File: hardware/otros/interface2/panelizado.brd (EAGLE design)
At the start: 85.9 x 92.1 mm, 40 parts

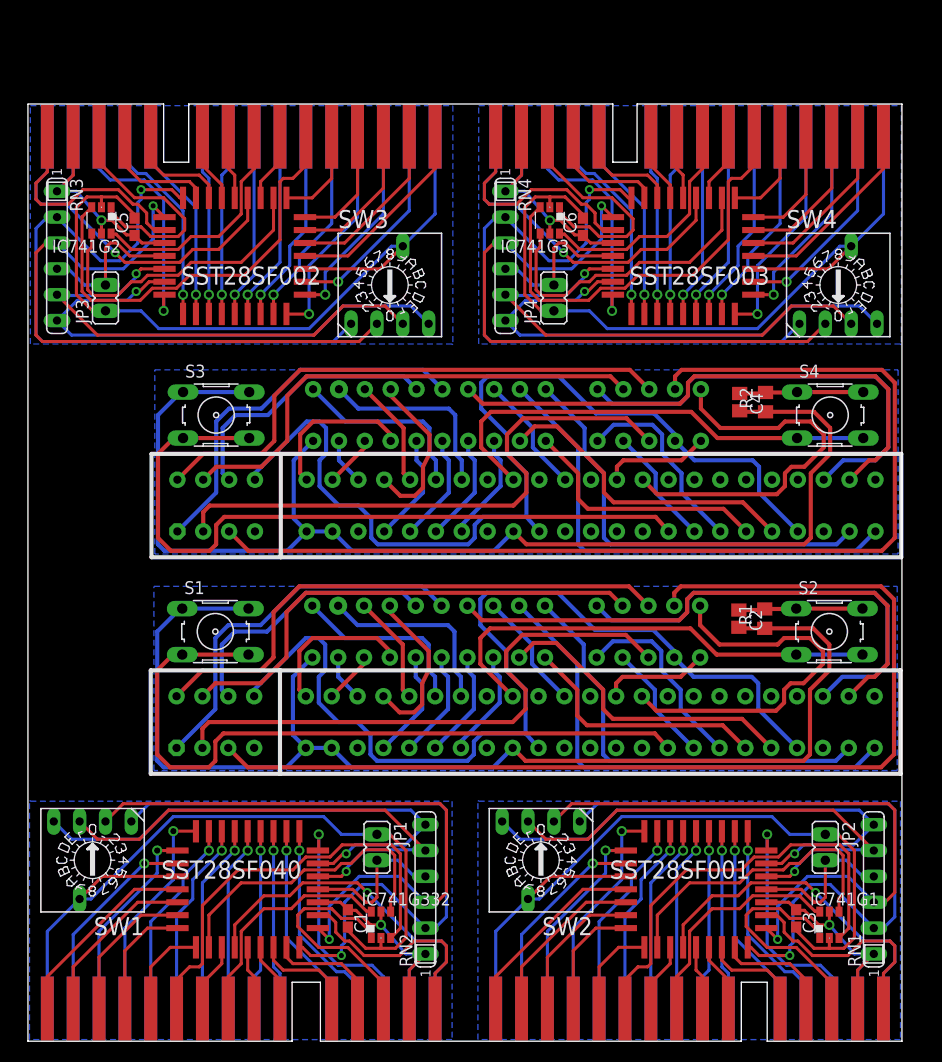
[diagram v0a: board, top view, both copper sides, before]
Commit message: 
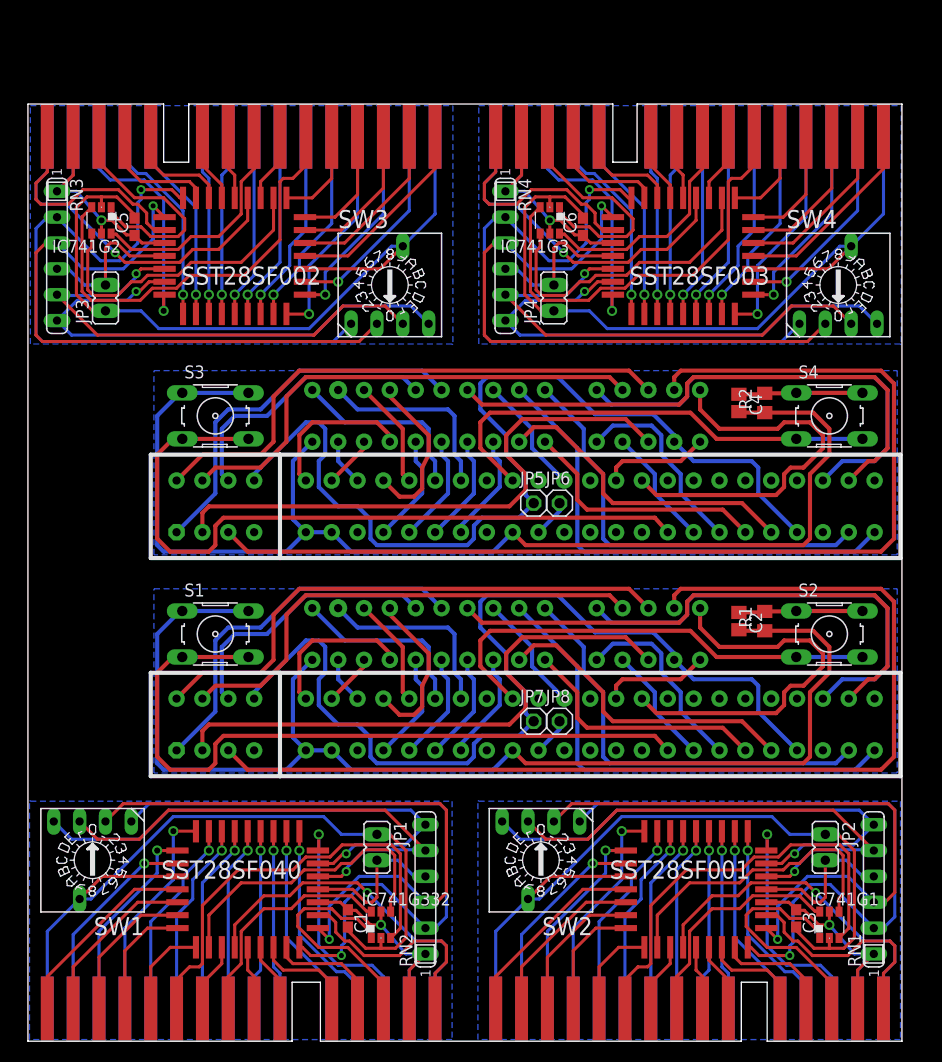
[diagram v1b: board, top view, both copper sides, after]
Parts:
- added JP5, JP6, JP7, JP8: (no value), pinhead:1X01
- moved C2 0.24 mm to (69.8, 41.3)
- moved R1 0.24 mm to (72.4, 41.3)
- moved S1 0.24 mm to (18.4, 40.0)
- moved S2 0.24 mm to (78.7, 40.0)
- moved U$2 0.24 mm to (45.7, 40.0)
- moved U$3 0.24 mm to (14.6, 33.7)
- moved C4 0.11 mm to (69.8, 62.7)
- moved R2 0.11 mm to (72.4, 62.7)
- moved S3 0.11 mm to (18.4, 61.4)
- moved S4 0.11 mm to (78.7, 61.4)
- moved U$5 0.11 mm to (14.6, 55.1)
- moved U$6 0.11 mm to (45.7, 61.4)
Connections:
- new net N$23: JP6.1, U$5.A15
- new net N$24: JP8.1, U$3.A15
- net ROMCS: now also JP7.1; no longer U$3.A15
- net ROMCS1: now also JP5.1; no longer U$5.A15
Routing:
- net N$23: track 0.00 -> 3.71 mm
- net N$24: track 0.00 -> 3.71 mm
- net ROMCS1: track 98.1 -> 96.5 mm
- net ROMCS: track 98.1 -> 96.5 mm
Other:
- board text added: "AntonioVillena"
- board text added: "Cartridge for IF2 AntonioVillena mar2015"
- board text added: "Interface II mar2015"

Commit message: 
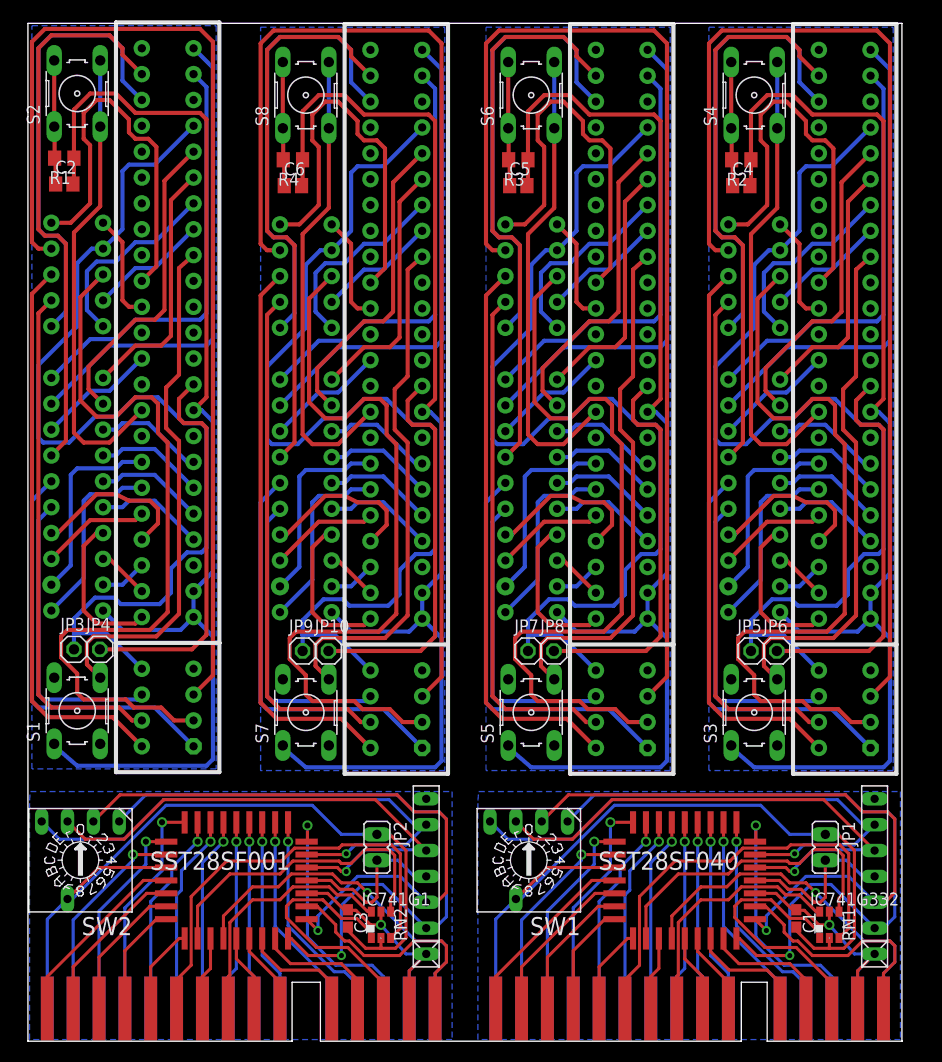
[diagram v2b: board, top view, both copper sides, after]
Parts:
- removed IC741G2, IC741G3: (no value), 74xx-little-de:DBV_R-PDSO-G6
- removed RN3, RN4: (no value), resistor-sil:SIL6
- removed SST28SF002, SST28SF003: (no value), memory:PLCC32R
- removed SW3, SW4: (no value), special:SW-C16
- added JP10, JP9: (no value), pinhead:1X01
- added R3, R4: 1K, rcl:R0805
- added S5, S6, S7, S8: (no value), switch-omron:B3F-10XX
- added U$10: ZX_CARTRIDGE, 8Bit_Parts:ZX_CARTRIDGE
- added U$9: (no value), zx_edge:2X28_SPE
- C2, C4: value 4.7nF -> 4.7uF
- C5, C6: value (none) -> 4.7uF; device rcl:C0603 -> resistor:C0805
- JP3, JP4: device jumper:JP1 -> pinhead:1X01
- RN1, RN2: device resistor-sil:SIL6 -> resistor-net:RN-7
- U$7: value IF2BUS -> (none); device SPECTRUM:BUS_CARTUCHO_IF2 -> zx_edge:2X28_SPE
- U$8: value IF2BUS -> ZX_CARTRIDGE; device SPECTRUM:BUS_CARTUCHO_IF2 -> 8Bit_Parts:ZX_CARTRIDGE
- moved S2 91.0 mm to (4.84, 93.1), turned to 90 degrees
- moved U$7 82.7 mm to (55.8, 28.8), turned to 90 degrees
- moved R1 82.5 mm to (3.57, 86.8), turned to 180 degrees
- moved C2 79.0 mm to (3.57, 84.2), turned to 0 degrees
- moved U$5 68.4 mm to (77.7, 28.8), turned to 90 degrees
- moved S3 60.4 mm to (71.4, 32.3), turned to 90 degrees
- moved JP4 56.4 mm to (7.06, 38.5)
- moved U$2 45.5 mm to (4.84, 60.1), turned to 90 degrees
- moved SW2 45.2 mm to (5.16, 17.8)
- moved SST28SF001 45.2 mm to (20.5, 15.8)
- moved JP1 44.1 mm to (78.3, 19.1)
- moved JP2 44.1 mm to (34.3, 19.1)
- moved U$1 44.1 mm to (83.4, 0.00)
- moved U$4 44.1 mm to (39.4, 0.00)
- moved C1 44.1 mm to (75.5, 12.1)
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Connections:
- removed net CS2: IC741G2.4, SST28SF002.22
- removed net CS3: IC741G3.4, SST28SF003.22
- removed net N$13 (its old number): JP3.2, RN3.4, SST28SF002.1
- removed net N$14 (its old number): RN3.3, SST28SF002.30, SW3.2
- removed net N$19: RN4.3, SST28SF003.30, SW4.2
- removed net N$20: RN4.5, SST28SF003.2, SW4.4
- removed net N$21: RN4.6, SST28SF003.3, SW4.8
- removed net N$22: RN4.2, SST28SF003.29, SW4.1
- removed net N$24: JP8.1, U$3.A15
- new net +12V2: U$7.B22
- new net +12V3: U$9.B22
- new net -12V2: U$7.B23
- new net -12V3: U$9.B23
- new net -5V2: U$7.B20
- new net -5V3: U$9.B20
- new net 9V2: U$7.A4
- new net 9V3: U$9.A4
- new net N$12: JP4.1, U$3.A15
- new net NMI2: S6.3, S6.4, U$7.B14
- new net NMI3: S8.3, S8.4, U$9.B14
- new net RESET2: S5.3, S5.4, U$7.A20
- new net RESET3: S7.3, S7.4, U$9.A20
- new net ROMCS2: JP7.1, U$7.A25, U$7.B4, U$8.ROMCS
- new net ROMCS3: JP9.1, U$10.ROMCS, U$9.A25, U$9.B4
- net A64: now also U$7.A1, U$8.A14; no longer SST28SF002.12, U$7.A0
- net A65: now also U$7.B27, U$8.A10; no longer IC741G2.3, U$7.A14
- net A66: now also U$7.A28, U$8.A11; no longer IC741G2.1, U$7.A15
- net A67: now also U$7.A27, U$8.A9; no longer SST28SF002.11, U$7.A1
- net A68: now also U$7.B26, U$8.A8; no longer SST28SF002.10, U$7.A2
- net A69: now also U$7.B2, U$8.A13; no longer SST28SF002.9, U$7.A3
- net A70: now also U$7.B1, U$8.A15; no longer SST28SF002.8, U$7.A4
- net A71: now also U$7.A9, U$8.A0; no longer SST28SF002.7, U$7.A5
- net A72: now also U$7.A10, U$8.A1; no longer SST28SF002.6, U$7.A6
- net A73: now also U$7.A11, U$8.A2; no longer SST28SF002.5, U$7.A7
- net A74: now also U$7.A12, U$8.A3; no longer SST28SF002.27, U$7.A8
- net A75: now also U$7.A24, U$8.A4; no longer SST28SF002.26, U$7.A9
- net A76: now also U$7.A23, U$8.A5; no longer SST28SF002.23, U$7.A10
- net A77: now also U$7.A22, U$8.A6; no longer SST28SF002.25, U$7.A11
- net A78: now also U$7.A21, U$8.A7; no longer SST28SF002.4, U$7.A12
- net A79: now also U$7.A2, U$8.A12; no longer SST28SF002.28, U$7.A13
- net A80: now also U$10.A14, U$9.A1; no longer SST28SF003.12, U$8.A0
- net A81: now also U$10.A10, U$9.B27; no longer IC741G3.3, U$8.A14
- net A82: now also U$10.A11, U$9.A28; no longer IC741G3.1, U$8.A15
- net A83: now also U$10.A9, U$9.A27; no longer SST28SF003.11, U$8.A1
- net A84: now also U$10.A8, U$9.B26; no longer SST28SF003.10, U$8.A2
- net A85: now also U$10.A13, U$9.B2; no longer SST28SF003.9, U$8.A3
- net A86: now also U$10.A15, U$9.B1; no longer SST28SF003.8, U$8.A4
- net A87: now also U$10.A0, U$9.A9; no longer SST28SF003.7, U$8.A5
- net A88: now also U$10.A1, U$9.A10; no longer SST28SF003.6, U$8.A6
- net A89: now also U$10.A2, U$9.A11; no longer SST28SF003.5, U$8.A7
- net A90: now also U$10.A3, U$9.A12; no longer SST28SF003.27, U$8.A8
- net A91: now also U$10.A4, U$9.A24; no longer SST28SF003.26, U$8.A9
- net A92: now also U$10.A5, U$9.A23; no longer SST28SF003.23, U$8.A10
- net A93: now also U$10.A6, U$9.A22; no longer SST28SF003.25, U$8.A11
- net A94: now also U$10.A7, U$9.A21; no longer SST28SF003.4, U$8.A12
- net A95: now also U$10.A12, U$9.A2; no longer SST28SF003.28, U$8.A13
- net D32: now also U$7.B11, U$8.D3; no longer SST28SF002.13, U$7.D0
- net D33: now also U$7.B12, U$8.D4; no longer SST28SF002.14, U$7.D1
- net D34: now also U$7.B10, U$8.D5; no longer SST28SF002.15, U$7.D2
- net D35: now also U$7.B9, U$8.D6; no longer SST28SF002.17, U$7.D3
- net D36: now also U$7.B3, U$8.D7; no longer SST28SF002.18, U$7.D4
- net D37: now also U$7.B8, U$8.D2; no longer SST28SF002.19, U$7.D5
- net D38: now also U$7.B7, U$8.D1; no longer SST28SF002.20, U$7.D6
- net D39: now also U$7.B6, U$8.D0; no longer SST28SF002.21, U$7.D7
- net D40: now also U$10.D3, U$9.B11; no longer SST28SF003.13, U$8.D0
- net D41: now also U$10.D4, U$9.B12; no longer SST28SF003.14, U$8.D1
- net D42: now also U$10.D5, U$9.B10; no longer SST28SF003.15, U$8.D2
- net D43: now also U$10.D6, U$9.B9; no longer SST28SF003.17, U$8.D3
- net D44: now also U$10.D7, U$9.B3; no longer SST28SF003.18, U$8.D4
- net D45: now also U$10.D2, U$9.B8; no longer SST28SF003.19, U$8.D5
- net D46: now also U$10.D1, U$9.B7; no longer SST28SF003.20, U$8.D6
- net D47: now also U$10.D0, U$9.B6; no longer SST28SF003.21, U$8.D7
- net GND4: now also R3.1, S5.1, S5.2, U$7.A14, U$7.A6, U$7.A7, U$8.GND; no longer IC741G2.2, JP3.1, SST28SF002.16, SW3.C, U$7.GND
- net GND5: now also R4.1, S7.1, S7.2, U$10.GND, U$9.A14, U$9.A6, U$9.A7; no longer IC741G3.2, JP4.1, SST28SF003.16, SW4.C, U$8.GND
- net MREQ4: now also U$7.B16, U$8.MREQ; no longer IC741G2.6, U$7.MREQ
- net MREQ5: now also U$10.MREQ, U$9.B16; no longer IC741G3.6, U$8.MREQ
- net N$10: now also RN2.6; no longer RN1.6
- net N$11: now also RN2.2; no longer RN1.2
- net N$15: now also C5.1, R3.2, S6.1, S6.2; no longer RN3.5, SST28SF002.2, SW3.4
- net N$16: now also JP8.1, U$7.A15; no longer RN3.6, SST28SF002.3, SW3.8
- net N$17: now also C6.1, R4.2, S8.1, S8.2; no longer RN3.2, SST28SF002.29, SW3.1
- net N$18: now also JP10.1, U$9.A15; no longer JP4.2, RN4.4, SST28SF003.1
- net N$2: now also RN1.4; no longer RN2.4
- net N$3: now also RN1.3; no longer RN2.3
- net N$4: now also RN1.5; no longer RN2.5
- net N$5: now also RN1.6; no longer RN2.6
- net N$6: now also RN1.2; no longer RN2.2
- net N$7: now also RN2.4; no longer RN1.4
- net N$8: now also RN2.3; no longer RN1.3
- net N$9: now also RN2.5; no longer RN1.5
- net RD4: now also U$7.B18, U$8.RD; no longer SST28SF002.24, U$7.RD
- net RD5: now also U$10.RD, U$9.B18; no longer SST28SF003.24, U$8.RD
- net ROMCS: now also JP3.1; no longer JP7.1
- net VCC: now also RN1.1; no longer RN2.1
- net VCC2: now also RN2.1; no longer RN1.1
- net VCC4: now also U$7.A3, U$8.+5V; no longer C5.1, IC741G2.5, RN3.1, SST28SF002.32, U$7.ROMCS, U$7.VCC
- net VCC5: now also U$10.+5V, U$9.A3; no longer C6.1, IC741G3.5, RN4.1, SST28SF003.32, U$8.ROMCS, U$8.VCC
- net WR4: now also U$7.B19, U$8.WR; no longer SST28SF002.31, U$7.WR
- net WR5: now also U$10.WR, U$9.B19; no longer SST28SF003.31, U$8.WR
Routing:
- net ROMCS3: track 0.00 -> 99.6 mm
- net ROMCS2: track 0.00 -> 99.6 mm
- net VCC4: track 26.2 -> 105.6 mm, vias 1 -> 0
- net VCC5: track 26.2 -> 105.6 mm, vias 1 -> 0
- net N$22: track 65.2 -> 0.00 mm, vias 1 -> 0
- net A79: track 11.7 -> 73.7 mm
- net A95: track 11.7 -> 73.7 mm
- net N$19: track 61.7 -> 0.00 mm, vias 1 -> 0
- net N$14 (its old number): track 61.7 -> 0.00 mm, vias 1 -> 0
- net N$17: track 65.2 -> 12.2 mm, vias 1 -> 0
- net N$21: track 51.2 -> 0.00 mm, vias 1 -> 0
- net RESET2: track 0.00 -> 51.1 mm
- net RESET3: track 0.00 -> 51.1 mm
- net N$20: track 49.4 -> 0.00 mm, vias 1 -> 0
- net NMI3: track 0.00 -> 46.0 mm
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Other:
- board size 85.9 x 92.1 mm -> 85.9 x 100 mm
- board text added: "AntonioVillena jul2015"
- board text added: "Cartridge for IF2"
- board text added: "Interface II jul2015"
- board text removed: "Cartridge for IF2 AntonioVillena mar2015"
- board text removed: "Interface II mar2015"
